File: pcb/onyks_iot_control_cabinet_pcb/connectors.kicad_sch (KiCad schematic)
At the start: 5 parts, among them J10 Conn_02x05_Odd_Even, J6 Conn_02x09_Odd_Even, J7 Screw_Terminal_01x02, J8 Conn_01x06_Pin, J9 Conn_01x02_Socket

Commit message: Add pins for the jumper and choosing the power supply; also add connection for JTAG 3V3
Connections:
- net +3.3V: now also J10.1 (Pin_1)
- no-connect marks 2 -> 1
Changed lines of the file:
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@@
-	)
-	(no_connect
-		(at 86.36 121.92)
 	)
 	(no_connect
@@
 		(pts
 			(xy 187.96 114.3) (xy 187.96 116.84)
+		)
+		(stroke
+			(width 0)
+			(type default)
+		)
+	)
+	(wire
+		(pts
+			(xy 81.28 121.92) (xy 86.36 121.92)
 		)
 		(stroke
@@
 					(unit 1)
 				)
+			)
+		)
+	)
+	(symbol
+		(lib_id "power:+3.3V")
+		(at 81.28 121.92 90)
+		(unit 1)
+		(exclude_from_sim no)
+		(in_bom yes)
+		(on_board yes)
+		(dnp no)
+		(property "Reference" "#PWR026"
+			(at 85.09 121.92 0)
+			(effects
+				(font
+					(size 1.27 1.27)
+				)
+				(hide yes)
+			)
+		)
+		(property "Value" "+3.3V"
+			(at 76.2 121.92 0)
+			(effects
+				(font
+					(size 1.27 1.27)
+				)
+			)
+		)
+		(property "Footprint" ""
+			(at 81.28 121.92 0)
+			(effects
+				(font
+					(size 1.27 1.27)
+				)
+				(hide yes)
+			)
+		)
+		(property "Datasheet" ""
+			(at 81.28 121.92 0)
+			(effects
+				(font
+					(size 1.27 1.27)
+				)
+				(hide yes)
+			)
+		)
+		(property "Description" ""
+			(at 81.28 121.92 0)
+			(effects
+				(font
+					(size 1.27 1.27)
+				)
+				(hide yes)
+			)
+		)
+		(pin "1"
+		)
+		(instances
+			(project "onyks_iot_control_cabinet_pcb"
+				(path "/789878cb-67d5-4bc7-a42d-b3bc72d661d0/9fa608f4-5282-4caa-ae1b-46582b97cb5d"
+					(reference "#PWR026")
+					(unit 1)
+				)

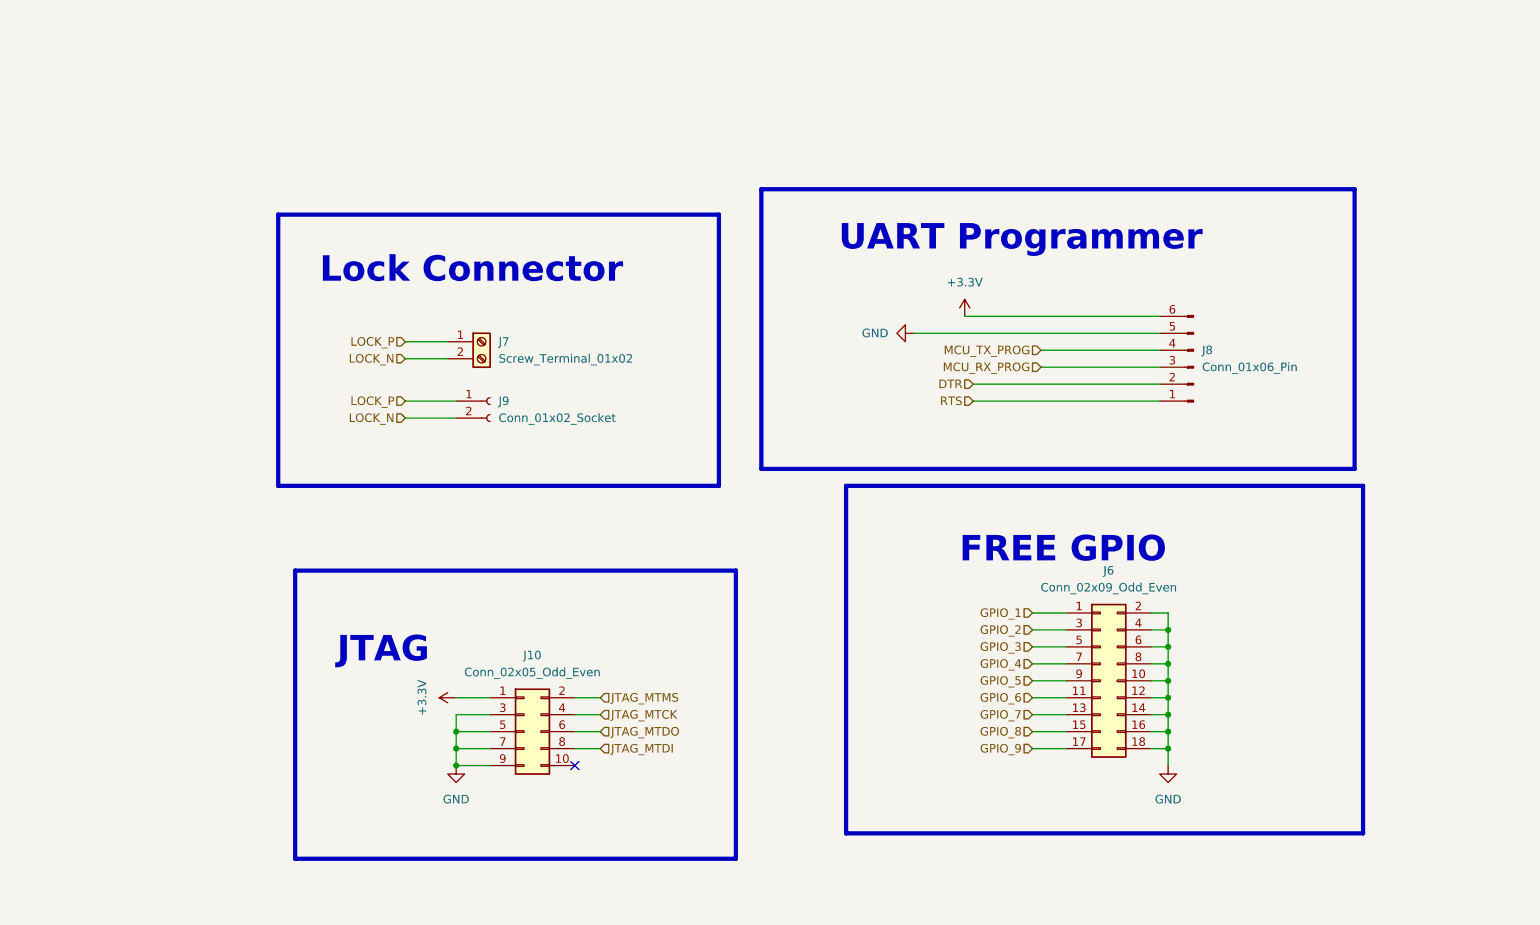
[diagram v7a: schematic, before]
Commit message: Karol can't add mounting holes/Added
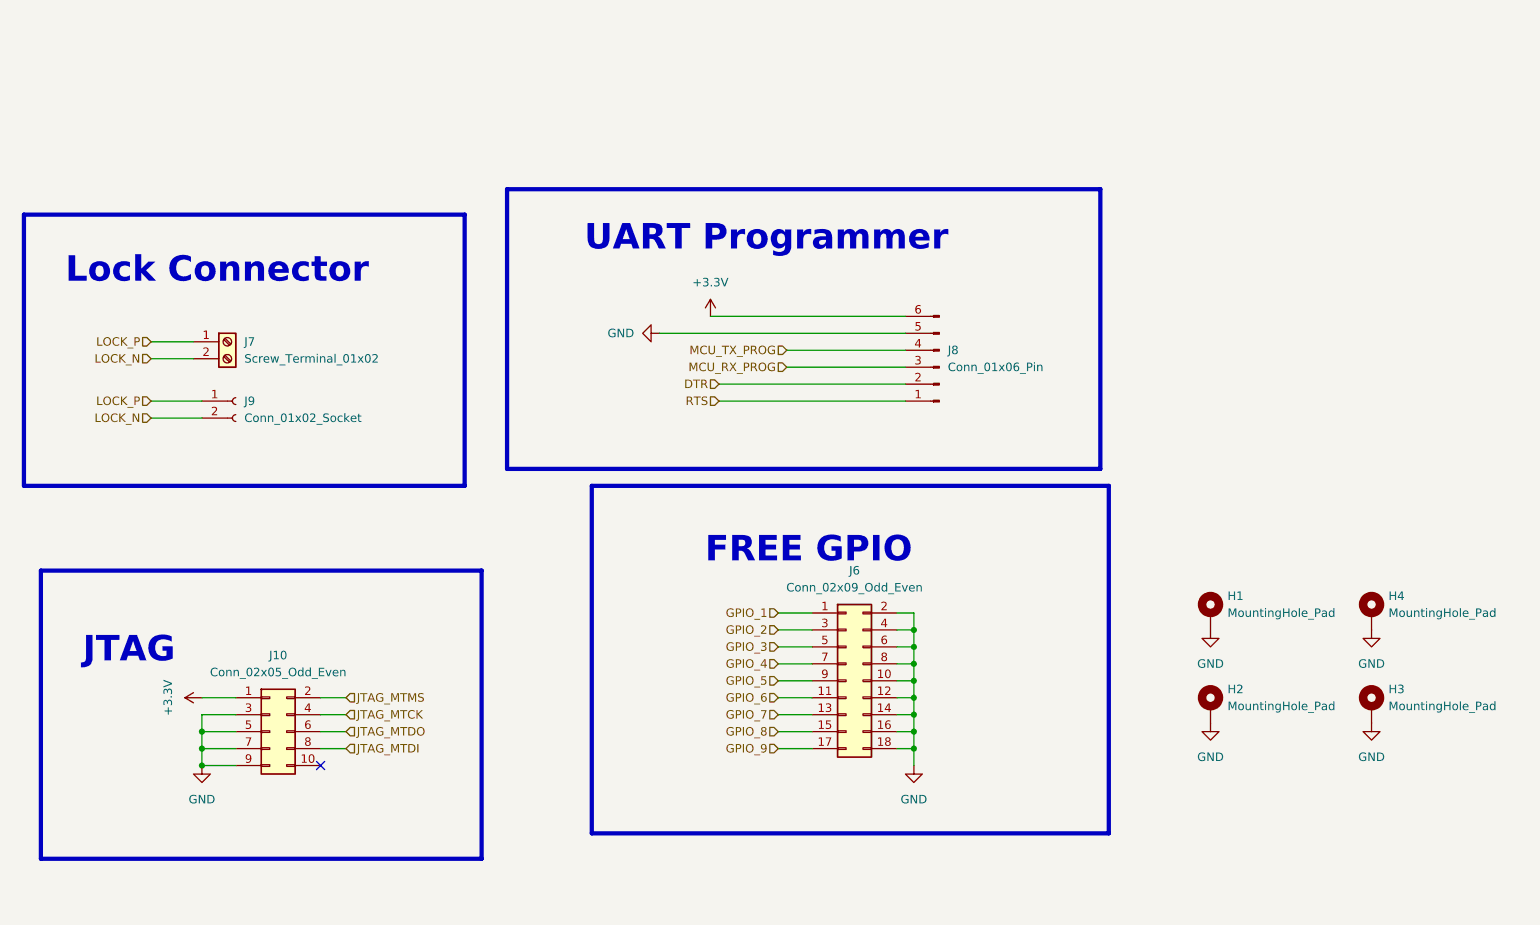
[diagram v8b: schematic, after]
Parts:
- added H1, H2, H3, H4: MountingHole_Pad, MountingHole:MountingHole_3.2mm_M3_DIN965_Pad_TopBottom, symbol Mechanical:MountingHole_Pad
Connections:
- net GND: now also H1.1, H2.1, H3.1, H4.1
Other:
- moved on the sheet: J10, J6, J7, J8, J9
